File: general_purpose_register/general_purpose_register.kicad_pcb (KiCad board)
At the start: 2 copper layers, 78.9 x 40.1 mm, 38 parts, among them J1 Power, J2 Control, J3 Data Bus, J4 ALU LHS, J5 ALU RHS, U1 74HCT574, U2 74HCT541, U3 74HCT541, U4 74HCT541

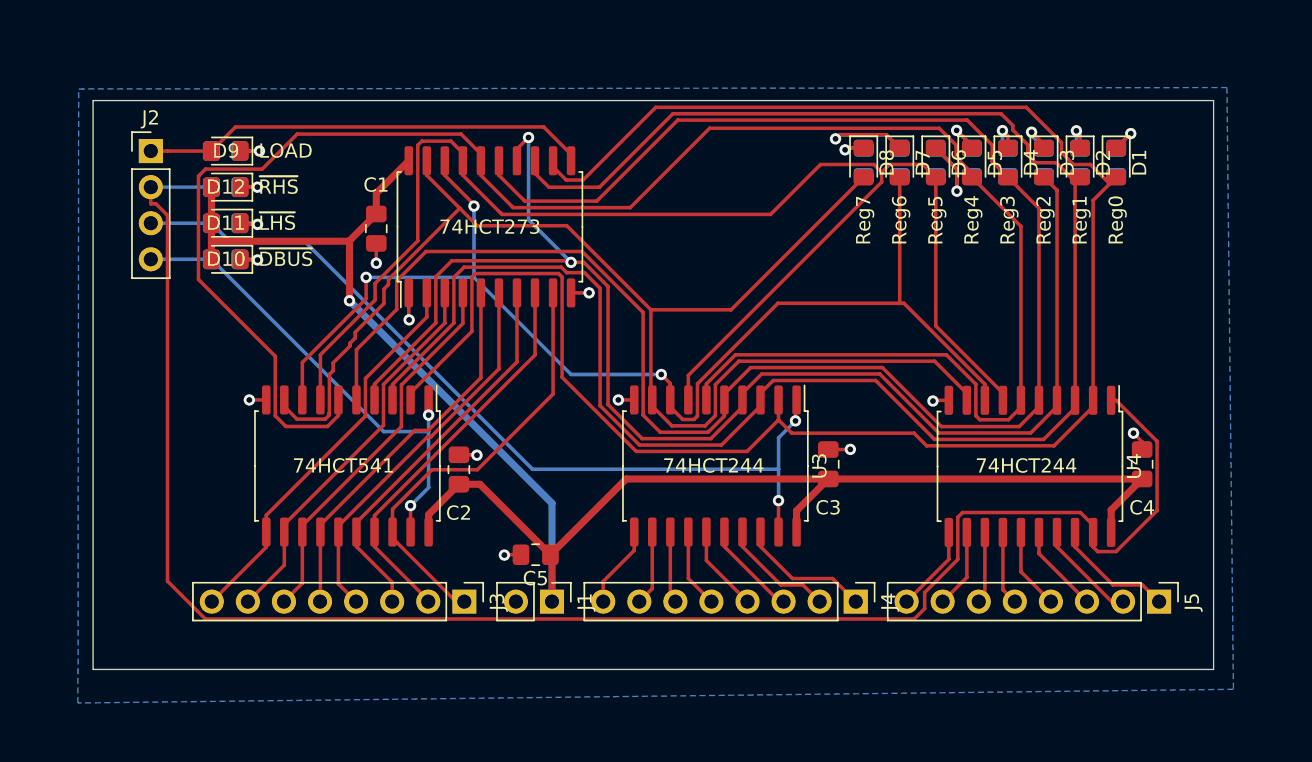
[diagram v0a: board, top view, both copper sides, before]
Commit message: Rerouted for better ground plane.
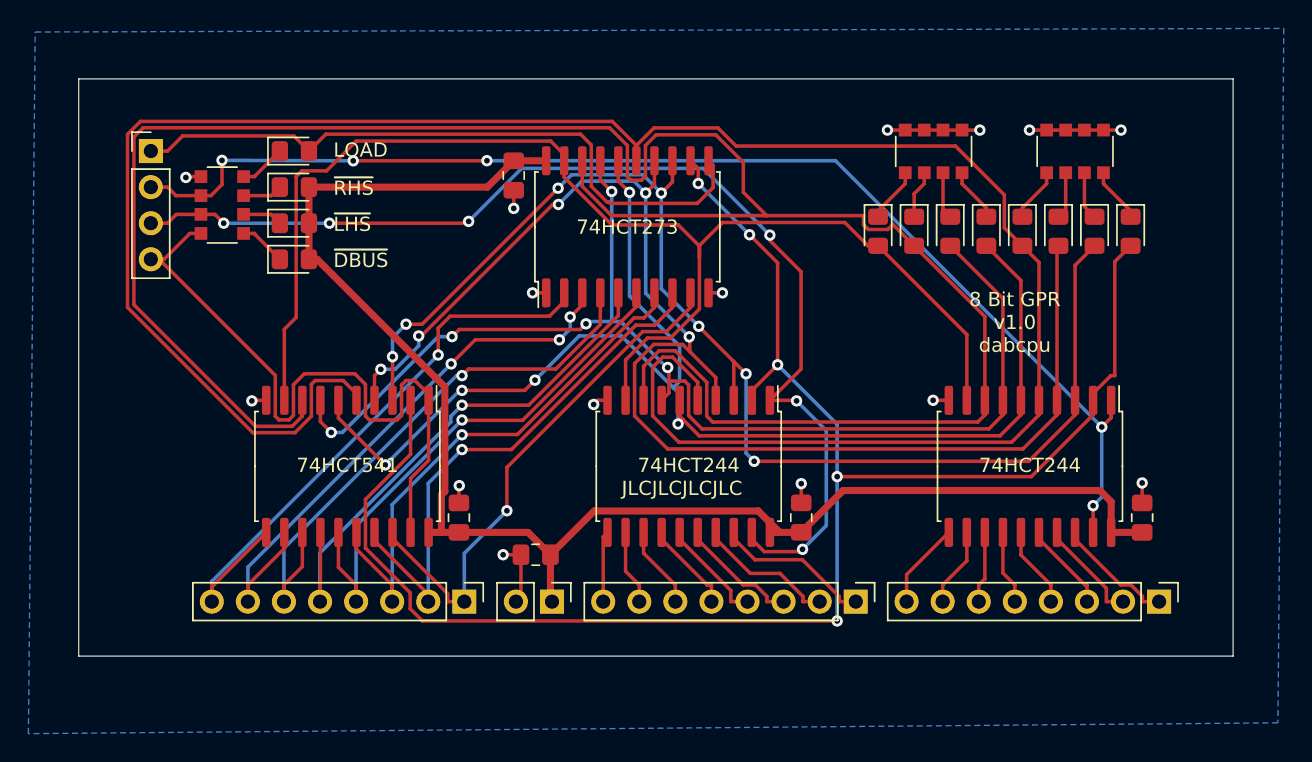
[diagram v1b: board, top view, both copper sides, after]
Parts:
- removed R1, R10, R11, R12, R2, R3, R4, R5, R6, R7, R8, R9: 1K, Resistor_SMD:R_0805_2012Metric_Pad1.20x1.40mm_HandSolder
- added RN1: 1k, Resistor_SMD:R_Array_Convex_4x1206, F.Cu at (119.9, 36.6)
- added RN2: 1k, Resistor_SMD:R_Array_Convex_4x1206, F.Cu at (110.0, 36.6)
- added RN3: 1k, Resistor_SMD:R_Array_Convex_4x1206, F.Cu at (59.9, 40.4)
- moved C1 10.4 mm to (80.4, 38.3)
- moved U1 9.68 mm to (88.4, 41.9)
- moved D9 9.01 mm to (65.0, 44.2), turned to 0 degrees
- moved D10 5.45 mm to (65.0, 41.7), turned to 0 degrees
- moved D11 5.45 mm to (65.0, 39.1), turned to 0 degrees
- moved D12 5.45 mm to (65.0, 36.6), turned to 0 degrees
- moved D2 4.93 mm to (121.3, 42.2)
- moved D4 4.93 mm to (116.2, 42.2)
- moved D6 4.93 mm to (111.2, 42.2)
- moved D7 4.93 mm to (108.6, 42.2)
- moved D1 4.93 mm to (123.8, 42.2)
- moved D3 4.93 mm to (118.8, 42.2)
- moved D5 4.93 mm to (113.7, 42.2)
- moved D8 4.93 mm to (106.1, 42.2)
- moved C3 4.21 mm to (100.7, 62.4)
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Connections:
- D12 pad 2: +5V -> /LOAD
- D9 pad 2: /LOAD -> +5V
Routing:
- net /REG6: track 85.3 -> 154.6 mm, vias 3 -> 0
- net /REG4: track 133.7 -> 91.9 mm, vias 0 -> 5
- net /REG1: track 129.3 -> 92.0 mm, vias 0 -> 7
- net /~RHS: track 121.5 -> 86.8 mm, vias 0 -> 5
- net /REG3: track 129.6 -> 156.2 mm
- net /~LHS: track 61.2 -> 79.1 mm, vias 2 -> 6
- net /REG5: track 102.0 -> 85.1 mm, vias 0 -> 5
- net +5V: track 122.8 -> 106.7 mm, vias 1 -> 0
- net GND: track 13.4 -> 29.2 mm, vias 10 -> 15
- net /LOAD: track 31.5 -> 47.2 mm
- net /DATA7: track 28.0 -> 42.7 mm, vias 0 -> 1
- net /DATA6: track 27.5 -> 40.9 mm, vias 0 -> 3
- net /~DBUS: track 34.4 -> 47.7 mm, vias 2 -> 0
- net /DATA5: track 27.0 -> 40.3 mm, vias 0 -> 1
- net /DATA4: track 27.0 -> 37.9 mm, vias 0 -> 1
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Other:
- board size 78.9 x 40.1 mm -> 81.3 x 40.6 mm
- board text added: "8 Bit GPR v1.0 dabcpu"
- board text added: "JLCJLCJLCJLC"
- board text removed: "Reg0"
- board text removed: "Reg1"
- board text removed: "Reg2"
- board text removed: "Reg3"
- board text removed: "Reg4"
- board text removed: "Reg5"
- board text removed: "Reg6"
- board text removed: "Reg7"
